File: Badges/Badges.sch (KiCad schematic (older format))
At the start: 30 parts

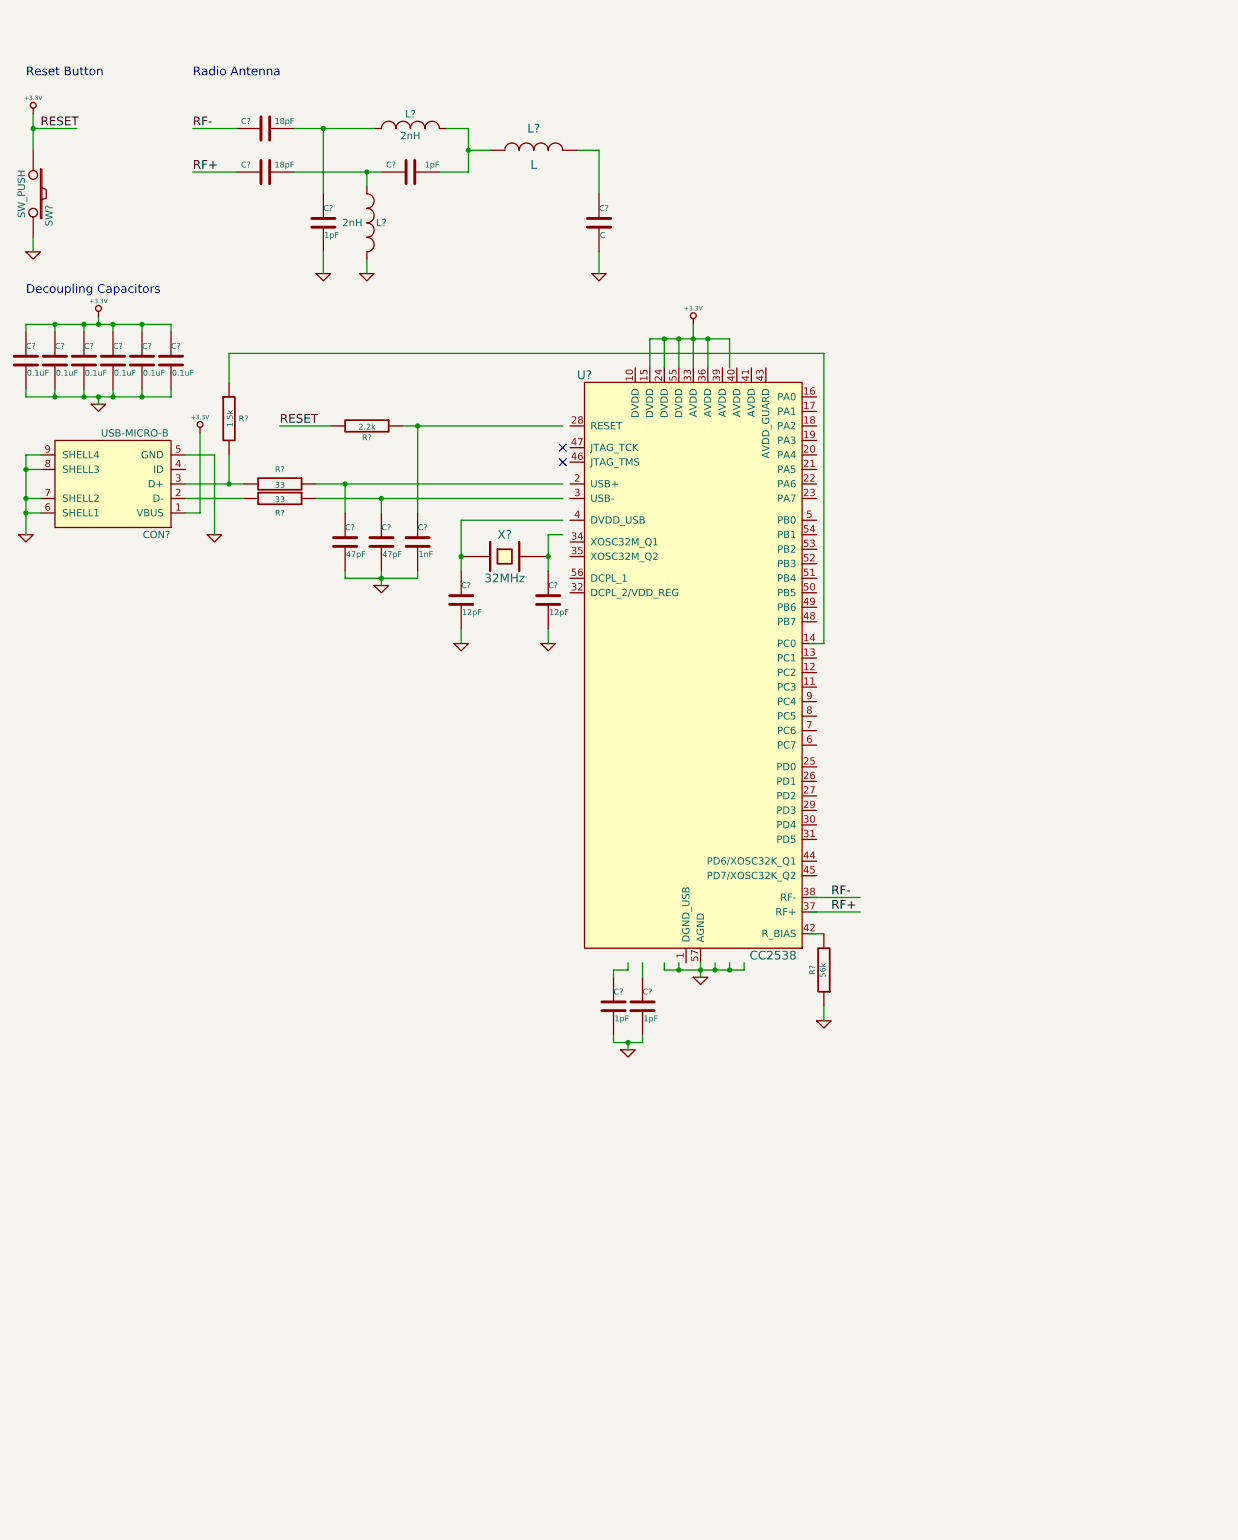
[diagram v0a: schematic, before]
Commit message: Completed RF and power
TODO: Add display device, buzzer, NFC/RFIC, battery
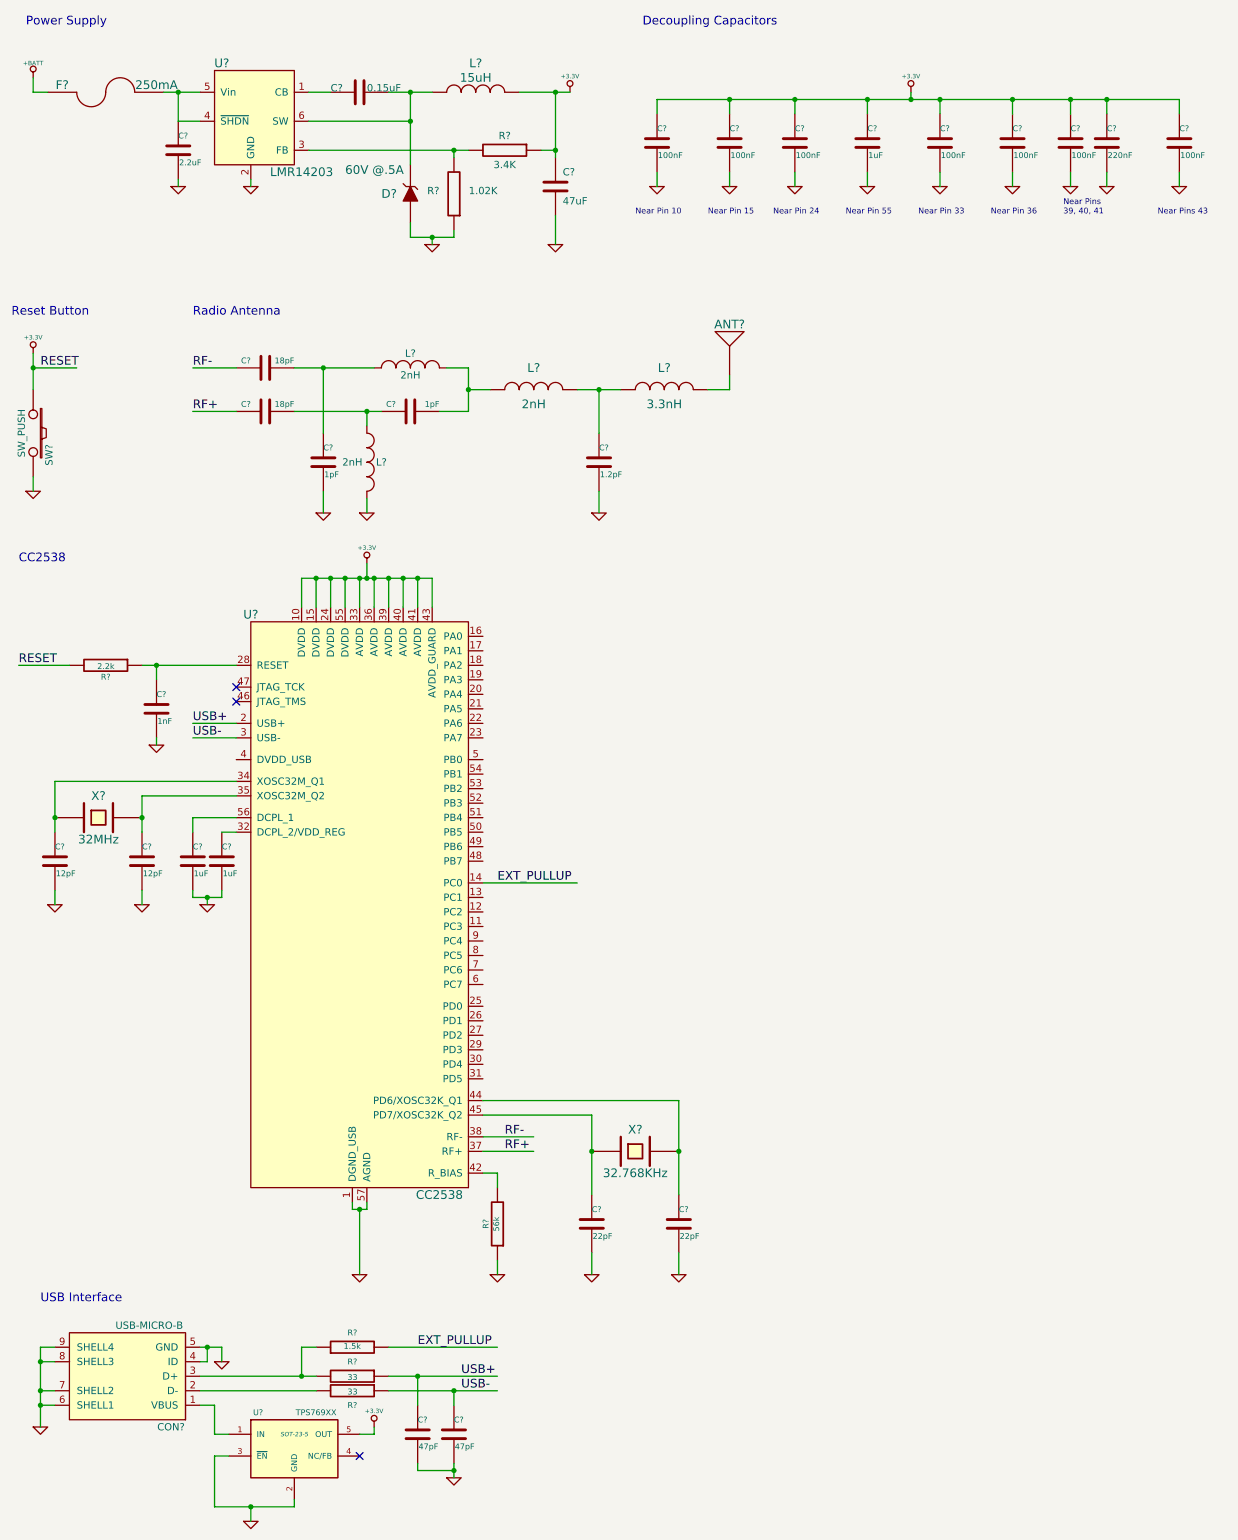
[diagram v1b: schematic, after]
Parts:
- removed C? (x6): 0.1uF, symbol C
- added ANT?: ANT-2.4-CHP, symbol ANT-2.4-CHP
- added C? (x2): 22pF, symbol C
- added C?: 0.15uF, Capacitors_SMD:C_0603_HandSoldering, symbol C
- added C?: 47uF, Capacitors_SMD:c_elec_6.3x5.8, symbol C
- added C?: 2.2uF, symbol C
- added C? (x7): 100nF, symbol C
- added C?: 1uF, symbol C
- added C?: 220nF, symbol C
- added D?: 60V @.5A, Diodes_SMD:Diode_SOT23_Handsoldering, symbol ZENER
- added F?: 250mA, Resistors_SMD:R_2512_HandSoldering, symbol PTC
- added L?: 3.3nH, symbol L
- added L?: 15uH, Solar_Car_lib:MOS6020, symbol L
- added R?: 3.4K, Resistors_SMD:R_0603_HandSoldering, symbol R
- added R?: 1.02K, Resistors_SMD:R_0603_HandSoldering, symbol R
- added U?: TPS769XX, SOT-23-5, symbol TPS769XX
- added U?: LMR14203, Solar_Car_lib:R-PDSO-G6, symbol LMR14203
- added X?: 32.768KHz, symbol CRYSTAL
- C? (x2): value 1pF -> 1uF
- C?: value C -> 1.2pF
- L?: value L -> 2nH
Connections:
- net labels added: +BATT, EXT_PULLUP, USB+, USB-
- wire segments 93 -> 139
- no-connect marks 2 -> 3
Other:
- note added: "CC2538"
- note added: "Near Pin 10"
- note added: "Near Pin 15"
- note added: "Near Pin 24"
- note added: "Near Pin 33"
- note added: "Near Pin 36"
- note added: "Near Pin 55"
- note added: "Near Pins 43"
- note added: "Near Pins \n39, 40, 41"
- note added: "Power Supply"
- note added: "USB Interface"
- moved on the sheet: C?, CON?, L?, R?, SW?, U?, X?
